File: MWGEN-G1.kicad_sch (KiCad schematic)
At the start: 36 parts, among them J101 Conn_01x02, Q101 BSS138, Q102 BSS138

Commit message: Footprint changes
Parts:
- removed R133, R134, R135, R136: 0R, Resistor_SMD:R_0805_2012Metric_Pad1.20x1.40mm_HandSolder, symbol Device:R
- added JP? (x4): SolderJumper_2_Open, Jumper:SolderJumper-2_P1.3mm_Open_TrianglePad1.0x1.5mm, symbol Jumper:SolderJumper_2_Open
- J101: value Conn_01x02 -> POWER
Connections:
- net GND: now also JP?.1 (A), JP?.1 (A), JP?.1 (A), JP?.1 (A)
- net at H101.1: now also JP?.2 (B)
- net at H103.1: now also JP?.2 (B)
- net at H104.1: now also JP?.2 (B)
- net at H102.1: now also JP?.2 (B)
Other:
- note added: "Isolatable mounting holes"

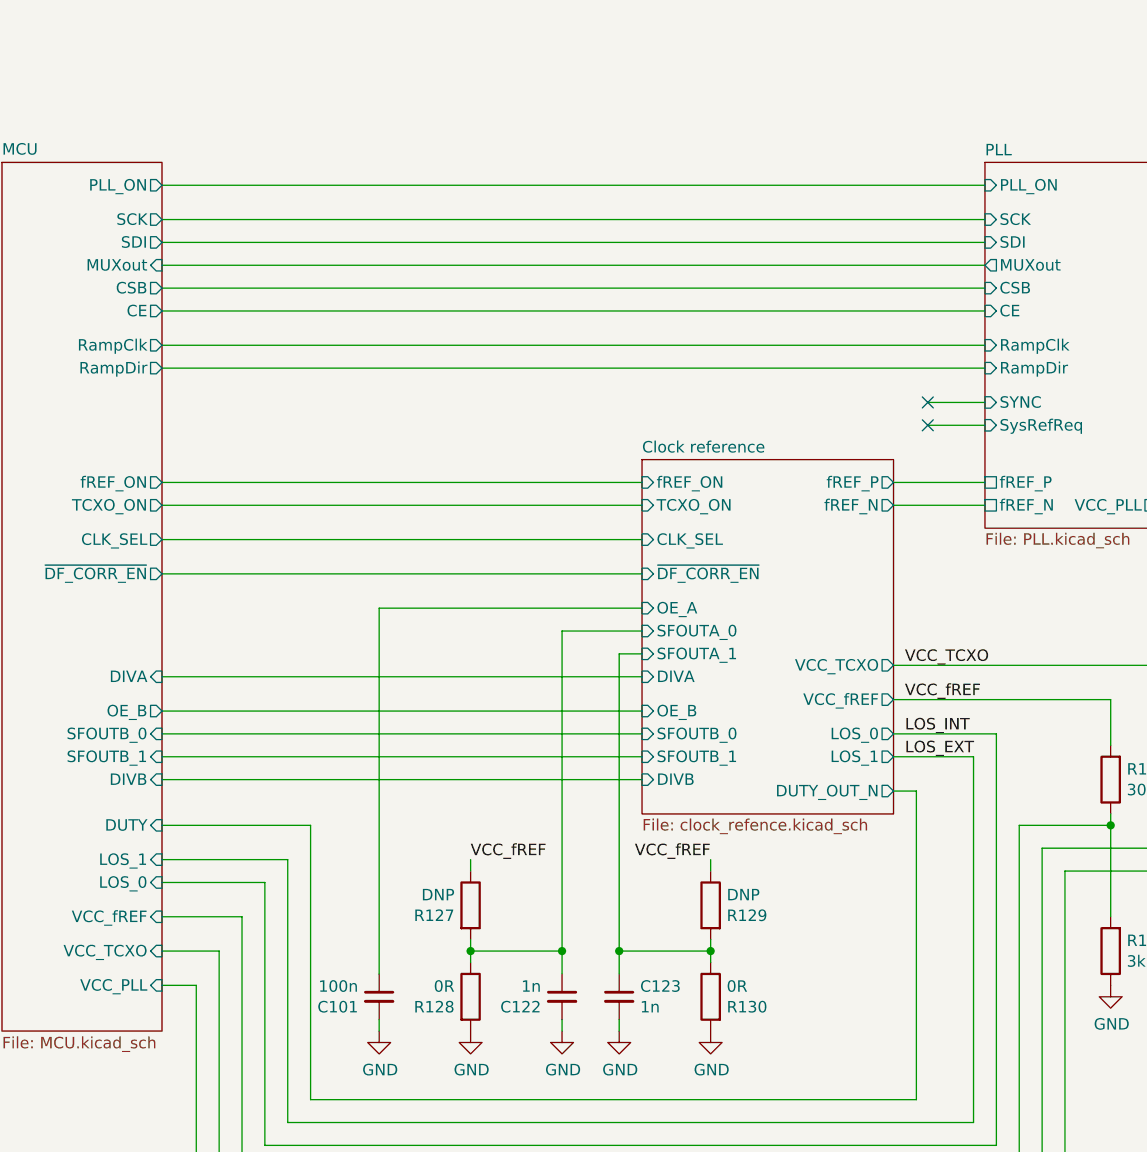
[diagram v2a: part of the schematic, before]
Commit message: Remade and simplified AUX/EXT section.
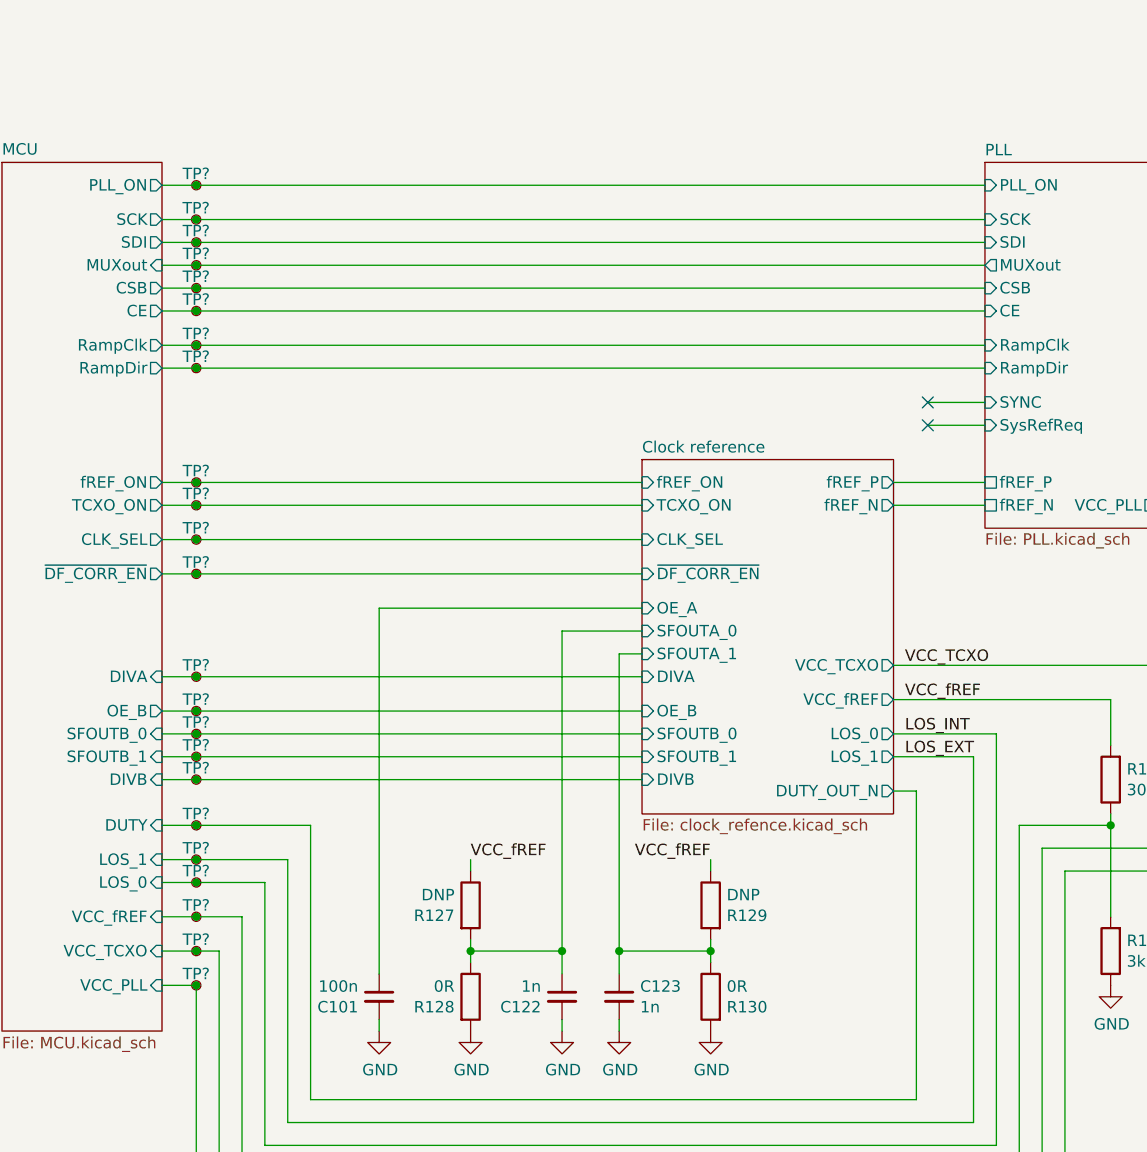
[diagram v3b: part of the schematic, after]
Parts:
- added TP? (x23): TestPoint_Small, symbol 4ms_Connector:TestPoint_Small
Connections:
- net Clock reference/CLK_SEL: now also TP?.1
- net Clock reference/DIVA: now also TP?.1
- net Clock reference/DIVB: now also TP?.1
- net Clock reference/DUTY_OUT_N: now also TP?.1
- net Clock reference/OE_B: now also TP?.1
- net Clock reference/SFOUTB_0: now also TP?.1
- net Clock reference/SFOUTB_1: now also TP?.1
- net Clock reference/TCXO_ON: now also TP?.1
- net Clock reference/fREF_ON: now also TP?.1
- net Clock reference/~{DF_CORR_EN}: now also TP?.1
- net LOS_EXT: now also TP?.1
- net LOS_INT: now also TP?.1
- net MCU/CE: now also TP?.1
- net MCU/CSB: now also TP?.1
- net MCU/MUXout: now also TP?.1
- net MCU/PLL_ON: now also TP?.1
- net MCU/RampClk: now also TP?.1
- net MCU/RampDir: now also TP?.1
- net MCU/SCK: now also TP?.1
- net MCU/SDI: now also TP?.1
- net MCU/VCC_PLL: now also TP?.1
- net MCU/VCC_TCXO: now also TP?.1
- net MCU/VCC_fREF: now also TP?.1

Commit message: Fixes.
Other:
- title: Generator 0.0125 - 6.4 GHz (0.02 - 9.8 GHz) -> Generator 0.0125 - 6.4 GHz (or up to 20 GHz)
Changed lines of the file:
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@@
   (paper "A4")
   (title_block
-    (title "Generator 0.0125 - 6.4 GHz (0.02 - 9.8 GHz)")
-    (date "2021-11-13")
-    (rev "211113-001")
+    (title "Generator 0.0125 - 6.4 GHz (or up to 20 GHz)")
+    (date "2021-12-30")
+    (rev "211230-001")
     (company "Petr Polasek")
-    (comment 1 "001, 2021-11-13 09:38")
-    (comment 2 "TCXO / external input, LMX2572/LMX2592")
-    (comment 3 "Dual channel symmetric outputs")
+    (comment 1 "001, 2021-12-30 00:50")
+    (comment 2 "TCXO / external input")
+    (comment 3 "LMX2572 (6.4 GHz) / LMX2592 (9.8GHz) / LMX2594 (15 GHz) / LMX2595 (20 GHz)")
+    (comment 4 "Dual channel symmetric outputs")
   )
   (junction (at 166.37 121.92) (diameter 0.9144) (color 0 0 0 0)
@@
       (reference "F101") (unit 1) (value "TODO") (footprint "Fuse:Fuse_2920_7451Metric_Pad2.10x5.45mm_HandSolder")
     )
+    (path "/94d4e8f5-2fc0-4789-8c71-9addd8579e30/0d57cc5e-2fdf-4fb8-a971-9a231aefc490"
+      (reference "F?") (unit 1) (value "TODO") (footprint "Fuse:Fuse_2920_7451Metric_Pad2.10x5.45mm_HandSolder")
+    )
     (path "/054d63ea-36d9-4b1e-bffd-240854122a36"
       (reference "FB101") (unit 1) (value "TODO") (footprint "Inductor_SMD:L_0805_2012Metric_Pad1.05x1.20mm_HandSolder")
@@
       (reference "TP?") (unit 1) (value "TestPoint_Small") (footprint "")
     )
-    (path "/94d4e8f5-2fc0-4789-8c71-9addd8579e30/51aaead8-3431-4d2b-a29a-4fbd9d607bd7"
+    (path "/94d4e8f5-2fc0-4789-8c71-9addd8579e30/53f10e28-c704-424c-bc01-21bca311b2c2"
       (reference "TP?") (unit 1) (value "TestPoint_Small") (footprint "")
     )

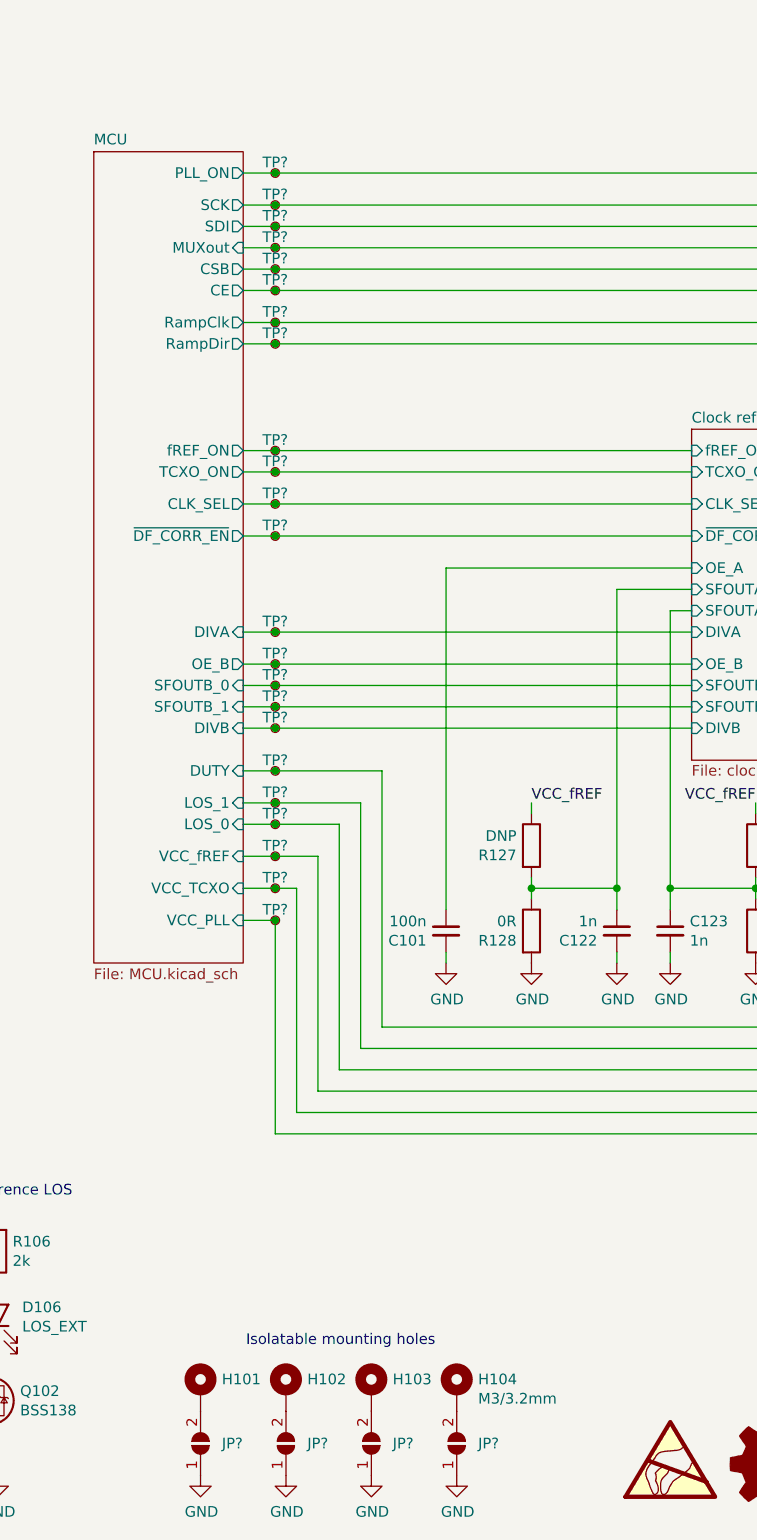
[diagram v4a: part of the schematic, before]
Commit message: Schematic ready for impoting changes into PCB.
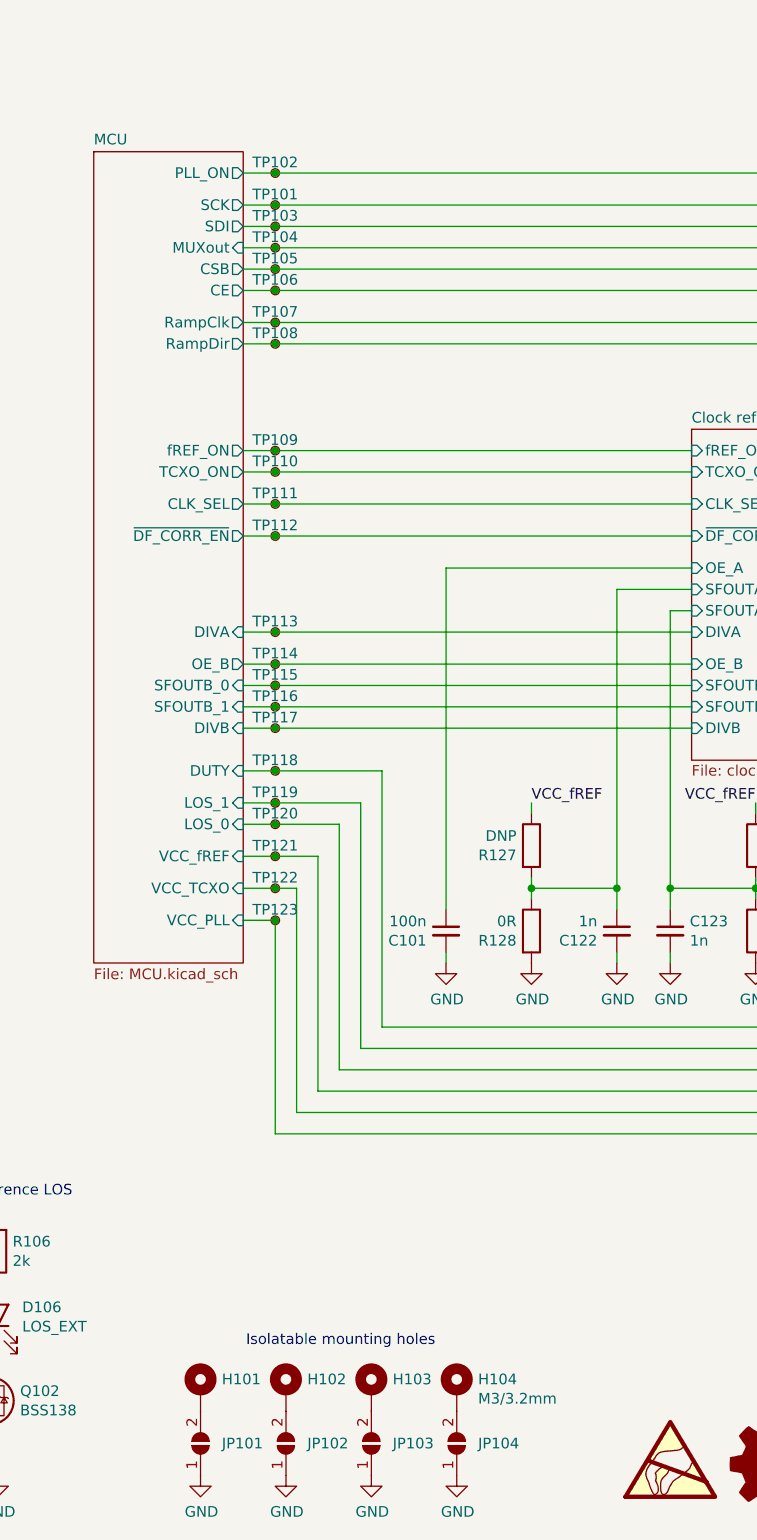
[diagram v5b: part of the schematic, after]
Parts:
- TP101, TP102, TP103, TP104, TP105, TP106, TP107, TP108, TP109, TP110, TP111, TP112, TP113, TP114, TP115, TP116, TP117, TP118, TP119, TP120, TP121, TP122, TP123: renamed from TP?; footprint (none) -> TestPoint:TestPoint_Pad_D1.0mm
- gave numbers to parts that had none: 4

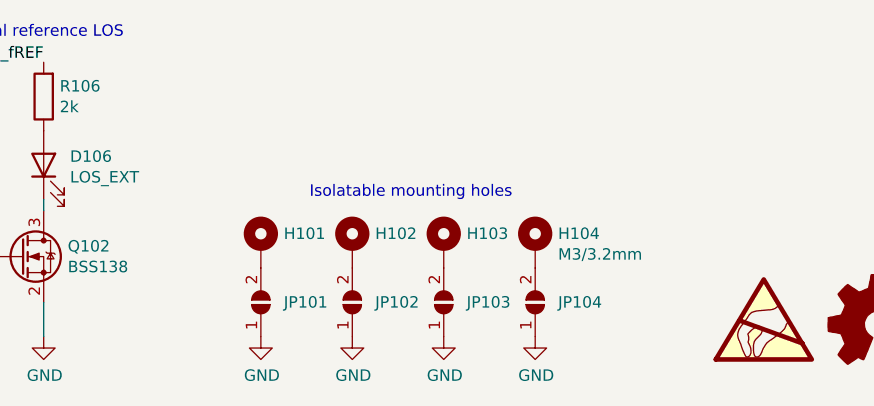
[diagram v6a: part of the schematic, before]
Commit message: Minor improvements and fixes to schematic, added high current LDO needed for high frequency PLLs.
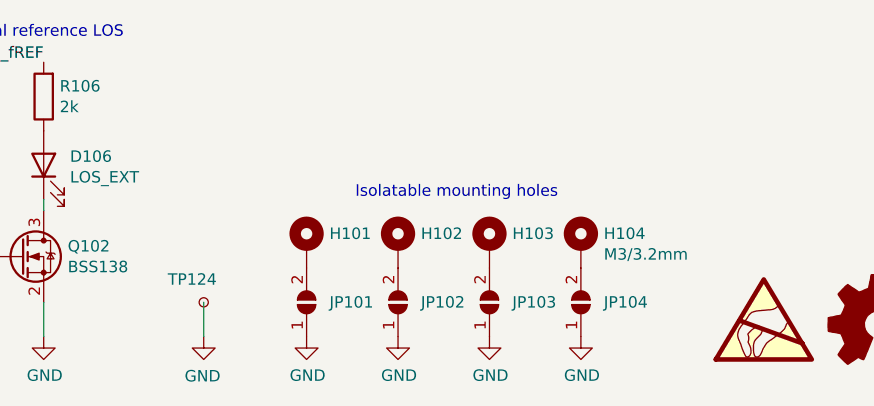
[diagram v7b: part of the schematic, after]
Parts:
- added TP124: TestPoint_Small, TestPoint:TestPoint_Pad_D1.0mm, symbol 4ms_Connector:TestPoint_Small
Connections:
- net GND: now also TP124.1
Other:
- moved on the sheet: H101, H102, H103, H104, JP101, JP102, JP103, JP104
